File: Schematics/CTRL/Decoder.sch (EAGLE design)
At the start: 187 parts

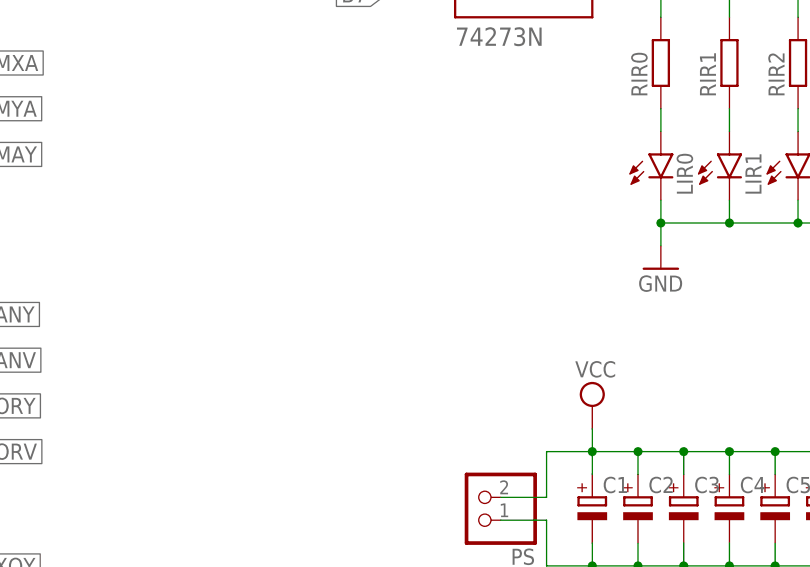
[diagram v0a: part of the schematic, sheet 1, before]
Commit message: IR reg now have cp pin
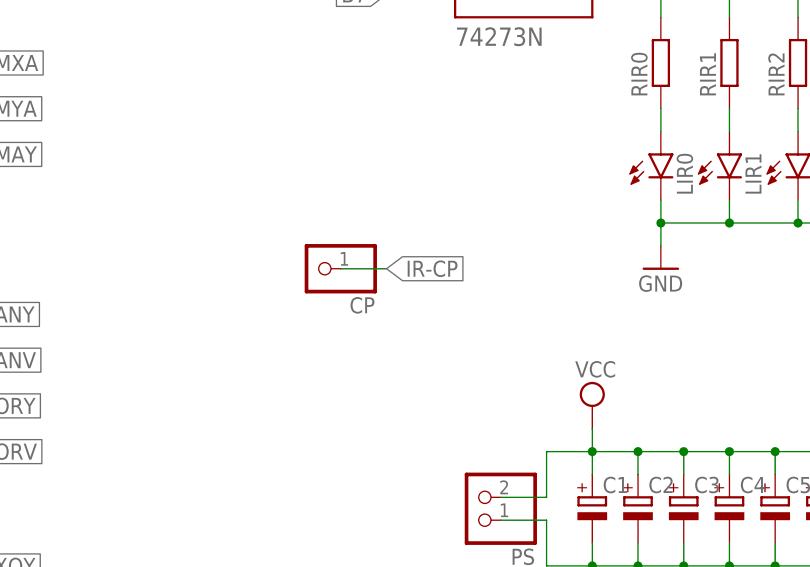
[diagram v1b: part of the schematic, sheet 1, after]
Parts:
- added CP: (no value), pinhead:PINHD-1X1
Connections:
- net IR-CP: now also CP.1
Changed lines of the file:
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@@
 <part name="GND16" library="supply1" library_urn="urn:adsk.eagle:library:371" deviceset="GND" device=""/>
 <part name="C11" library="rcl" library_urn="urn:adsk.eagle:library:334" deviceset="CPOL-EU" device="E2.5-6" package3d_urn="urn:adsk.eagle:package:23349/1"/>
+<part name="CP" library="pinhead" library_urn="urn:adsk.eagle:library:325" deviceset="PINHD-1X1" device="" package3d_urn="urn:adsk.eagle:package:22485/2"/>
 </parts>
 <sheets>
@@
 <attribute name="NAME" x="227.203" y="58.9026" size="1.778" layer="95"/>
 <attribute name="VALUE" x="227.203" y="53.8226" size="1.778" layer="96"/>
+</instance>
+<instance part="CP" gate="G$1" x="144.78" y="83.82" smashed="yes" rot="R180">
+<attribute name="NAME" x="151.13" y="80.645" size="1.778" layer="95" rot="R180"/>
+<attribute name="VALUE" x="151.13" y="88.9" size="1.778" layer="96" rot="R180"/>
 </instance>
 </instances>
@@
 <label x="152.4" y="157.48" size="1.778" layer="95" rot="R180" xref="yes"/>
 </segment>
-</net>
+<segment>
+<pinref part="CP" gate="G$1" pin="1"/>
+<wire x1="152.4" y1="83.82" x2="147.32" y2="83.82" width="0.1524" layer="91"/>
+<label x="152.4" y="83.82" size="1.778" layer="95" xref="yes"/>
+</segment>
+</net>
